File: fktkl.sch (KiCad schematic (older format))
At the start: 157 parts, among them K1 Esc, K10 Super, K11 2, K12 W, K13 S, K14 X, K15 Alt, K16 3, K17 E, K18 D, K19 C, K2 Tab, K20 4, K21 R, K22 F, K23 V, K24 5, K25 T, K26 G, K27 B, K28 6, K29 Y, K3 Caps, K3.1 SCaps, K30 H, K31 N, K32 Space, K33 7, K34 U, K35 J, K36 M, K37 8, K38 I, K39 K, K4 Shift, K40 ,, K41 9, K42 O, K43 L, K44 ., K45 0, K46 P, K47 ;, K48 /, K49 Ctrl, K5 Ctrl, K50 -, K51 [, K52 ', K53 =, K54 ], K55 Shift, K56 Win, K57 Yen, K58 BS1, K59 BS2, K6 1, K60 \\, K61 Enter, K62 Fn, K63 AltGr, K64 Ins, K65 Del, K66 C0, K67 C3, K68 Left, K69 Home, K7 Q, K70 End, K71 C1, K72 Up, K73 Down, K74 PgUp, K75 PgDwn, K76 C2, K77 C4, K78 Right, K8 A, K9 Z, U1 TEENSY2.0

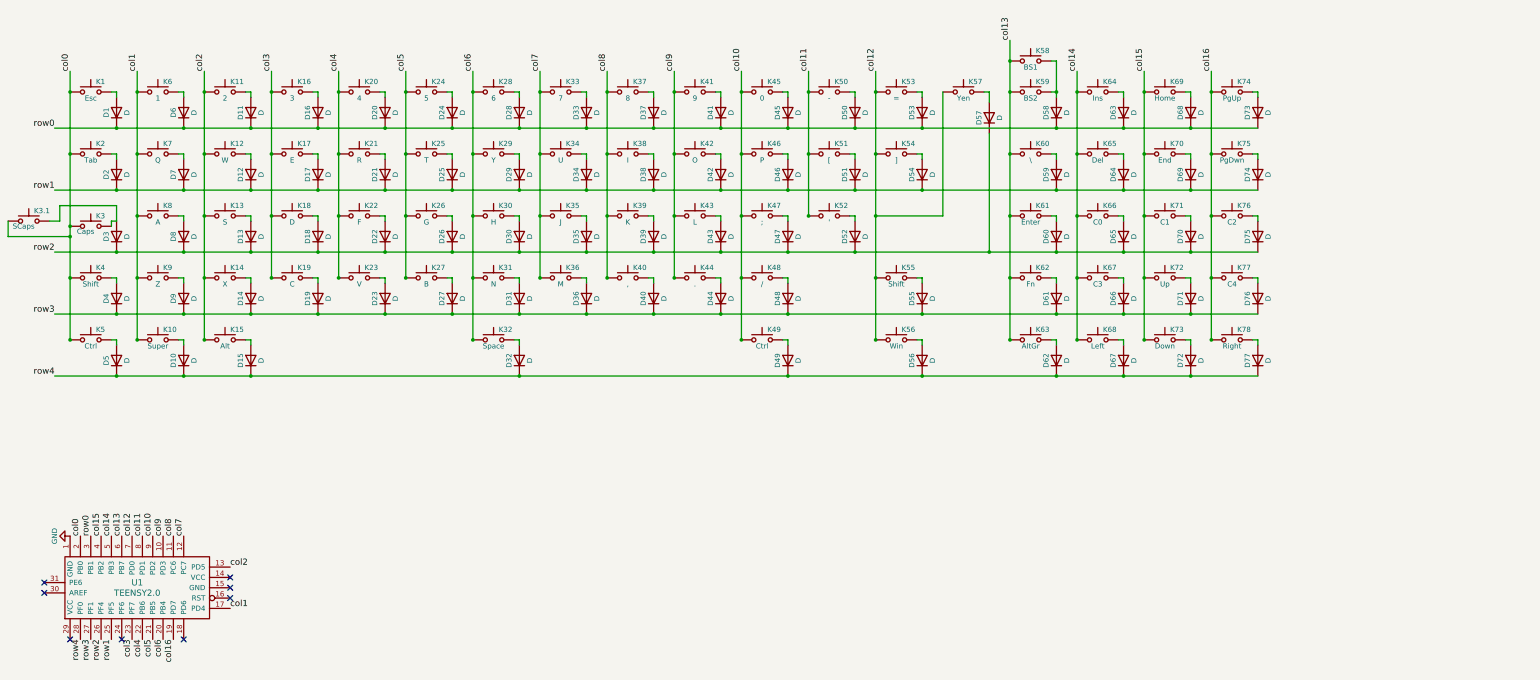
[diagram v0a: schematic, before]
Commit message: changed controller to pro micro
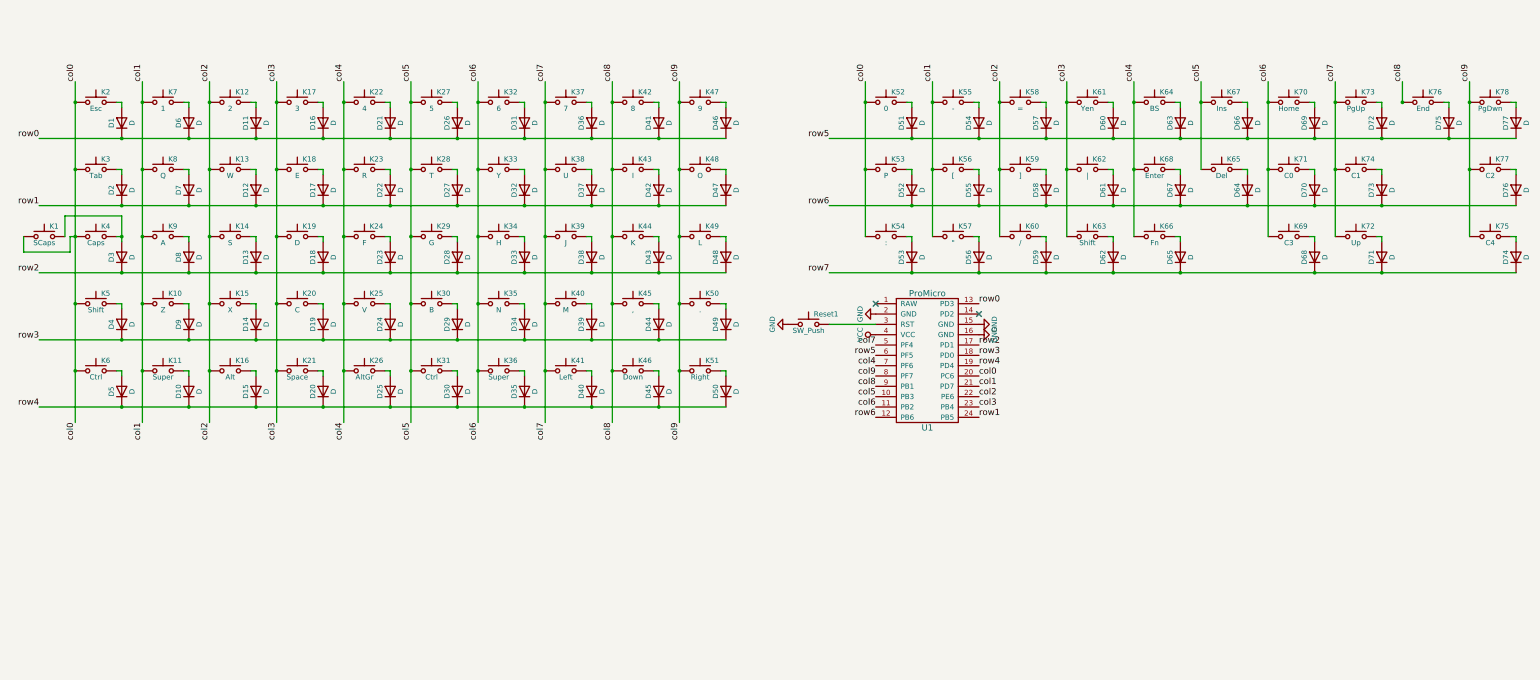
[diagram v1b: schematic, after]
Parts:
- removed K3.1: SCaps, canadian_footprints:Mx_Alps_125, symbol SW_Push
- removed U1: TEENSY2.0, jan_footprints:Teensy_20_wo_front_text, symbol TEENSY2.0
- added Reset1: SW_Push, canadian_footprints:SW_TACT_ALPS_SKQGABE010, symbol SW_Push
- added U1: ProMicro, canadian_footprints:Pro_Micro, symbol ProMicro
- K1: value Esc -> SCaps; footprint canadian_footprints:Mx_Alps_100 -> canadian_footprints:Mx_Alps_125
- K10: value Super -> Z
- K11: value 2 -> Super
- K12: value W -> 2
- K13: value S -> W
- K14: value X -> S
- K15: value Alt -> X; footprint canadian_footprints:Mx_Alps_150 -> canadian_footprints:Mx_Alps_100
- K16: value 3 -> Alt; footprint canadian_footprints:Mx_Alps_100 -> canadian_footprints:Mx_Alps_150
- K17: value E -> 3
- K18: value D -> E
- K19: value C -> D
- K2: value Tab -> Esc; footprint canadian_footprints:Mx_Alps_150 -> canadian_footprints:Mx_Alps_100
- K20: value 4 -> C
- K21: value R -> Space; footprint canadian_footprints:Mx_Alps_100 -> MX_Alps_Hybrid:MX-7U-ReversedStabilizers-NoLED
- K22: value F -> 4
- K23: value V -> R
- K24: value 5 -> F
- K25: value T -> V
- K26: value G -> AltGr; footprint canadian_footprints:Mx_Alps_100 -> canadian_footprints:Mx_Alps_150
- K27: value B -> 5
- K28: value 6 -> T
- K29: value Y -> G
- K3: value Caps -> Tab; footprint canadian_footprints:Mx_Alps_175 -> canadian_footprints:Mx_Alps_150
- K30: value H -> B
- K31: value N -> Ctrl; footprint canadian_footprints:Mx_Alps_100 -> canadian_footprints:Mx_Alps_150
- K32: value Space -> 6; footprint MX_Alps_Hybrid:MX-7U-ReversedStabilizers-NoLED -> canadian_footprints:Mx_Alps_100
- K33: value 7 -> Y
- K34: value U -> H
- K35: value J -> N
- K36: value M -> Super
- K37: value 8 -> 7
- K38: value I -> U
- K39: value K -> J
- K4: value Shift -> Caps; footprint canadian_footprints:Mx_Alps_225 -> canadian_footprints:Mx_Alps_175
- K40: value , -> M
- K41: value 9 -> Left
- K42: value O -> 8
- K43: value L -> I
- K44: value . -> K
- K45: value 0 -> ,
- K46: value P -> Down
- K47: value ; -> 9
- K48: value / -> O
- K49: value Ctrl -> L; footprint canadian_footprints:Mx_Alps_150 -> canadian_footprints:Mx_Alps_100
- K5: value Ctrl -> Shift; footprint canadian_footprints:Mx_Alps_150 -> canadian_footprints:Mx_Alps_225
- K50: value - -> .
- K51: value [ -> Right
- K52: value ' -> 0
- K53: value = -> P
- K54: value ] -> :
- K55: value Shift -> -; footprint canadian_footprints:Mx_Alps_175 -> canadian_footprints:Mx_Alps_100
- K56: value Win -> [
- K57: value Yen -> \"
- K58: value BS1 -> =
- K59: value BS2 -> ]; footprint canadian_footprints:Mx_Alps_200 -> canadian_footprints:Mx_Alps_100
- K6: value 1 -> Ctrl; footprint canadian_footprints:Mx_Alps_100 -> canadian_footprints:Mx_Alps_150
- K60: value \\ -> /; footprint canadian_footprints:Mx_Alps_150 -> canadian_footprints:Mx_Alps_100
- K61: value Enter -> Yen; footprint canadian_footprints:Mx_Alps_225 -> canadian_footprints:Mx_Alps_100
- K62: value Fn -> |; footprint canadian_footprints:Mx_Alps_100 -> canadian_footprints:Mx_Alps_150
- K63: value AltGr -> Shift; footprint canadian_footprints:Mx_Alps_150 -> canadian_footprints:Mx_Alps_175
- K64: value Ins -> BS
- K66: value C0 -> Fn
- K67: value C3 -> Ins
- K68: value Left -> Enter; footprint canadian_footprints:Mx_Alps_100 -> canadian_footprints:Mx_Alps_225
- K69: value Home -> C3
- K7: value Q -> 1
- K70: value End -> Home
- K71: value C1 -> C0
- K73: value Down -> PgUp
- K74: value PgUp -> C1
- K75: value PgDwn -> C4
- K76: value C2 -> End
- K77: value C4 -> C2
- K78: value Right -> PgDwn
- K8: value A -> Q
- K9: value Z -> A
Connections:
- net GND: now also Reset1.1, U1.15 (GND), U1.16 (GND), U1.2 (GND)
- net col0: now also K52.1, K53.1, K54.1, K6.1, U1.20 (PC6)
- net col1: now also K11.1, K55.1, K56.1, K57.1, U1.21 (PD7); no longer K6.1
- net col2: now also K16.1, K58.1, K59.1, K60.1, U1.22 (PE6); no longer K11.1
- net col3: now also K20.1, K21.1, K61.1, K62.1, K63.1, U1.23 (PB4); no longer K16.1
- net col4: now also K24.1, K25.1, K26.1, K64.1, K66.1, K68.1, U1.7 (PF6); no longer K20.1, K21.1
- net col5: now also K28.1, K29.1, K30.1, K31.1, K65.1, K67.1, U1.10 (PB3); no longer K24.1, K25.1, K26.1
- net col6: now also K33.1, K34.1, K35.1, K36.1, K69.1, K70.1, K71.1, U1.11 (PB2); no longer K28.1, K29.1, K30.1, K31.1
- net col7: now also K37.1, K38.1, K39.1, K40.1, K41.1, K72.1, K73.1, K74.1, U1.5 (PF4); no longer K33.1, K34.1, K35.1, K36.1
- net col8: now also K42.1, K43.1, K44.1, K45.1, K46.1, K76.1, U1.9 (PB1); no longer K37.1, K38.1, K39.1, K40.1
- net col9: now also K47.1, K48.1, K49.1, K50.1, K51.1, K75.1, K77.1, K78.1, U1.8 (PF7); no longer K41.1, K42.1, K43.1, K44.1
- net row0: now also D21.1 (K), D26.1 (K), D31.1 (K), D36.1 (K), D46.1 (K), U1.13 (PD3); no longer D20.1 (K), D24.1 (K), D28.1 (K), D33.1 (K), D37.1 (K), D45.1 (K), D50.1 (K), D53.1 (K), D58.1 (K), D63.1 (K), D68.1 (K), D73.1 (K)
- net row1: now also D22.1 (K), D27.1 (K), D32.1 (K), D37.1 (K), D47.1 (K), U1.24 (PB5); no longer D21.1 (K), D25.1 (K), D29.1 (K), D34.1 (K), D38.1 (K), D46.1 (K), D51.1 (K), D54.1 (K), D59.1 (K), D64.1 (K), D69.1 (K), D74.1 (K)
- net row2: now also D23.1 (K), D28.1 (K), D33.1 (K), D38.1 (K), D48.1 (K), U1.17 (PD1); no longer D22.1 (K), D26.1 (K), D30.1 (K), D35.1 (K), D39.1 (K), D47.1 (K), D52.1 (K), D57.1 (K), D60.1 (K), D65.1 (K), D70.1 (K), D75.1 (K)
- net row3: now also D24.1 (K), D29.1 (K), D34.1 (K), D39.1 (K), D49.1 (K), U1.18 (PD0); no longer D23.1 (K), D27.1 (K), D31.1 (K), D36.1 (K), D40.1 (K), D48.1 (K), D55.1 (K), D61.1 (K), D66.1 (K), D71.1 (K), D76.1 (K)
- net row4: now also D20.1 (K), D25.1 (K), D30.1 (K), D35.1 (K), D40.1 (K), D45.1 (K), D50.1 (K), U1.19 (PD4); no longer D32.1 (K), D49.1 (K), D56.1 (K), D62.1 (K), D67.1 (K), D72.1 (K), D77.1 (K)
- net at K2.2: now also D1.2 (A); no longer D2.2 (A)
- net at K1.2: now also D3.2 (A), K4.2; no longer D1.2 (A)
- net at D4.2 (A): now also K5.2; no longer K4.2
- net at K3.2: now also D2.2 (A); no longer D3.2 (A)
- net at D5.2 (A): now also K6.2; no longer K5.2
- net at K7.2: now also D6.2 (A); no longer D7.2 (A)
- net at K9.2: now also D8.2 (A); no longer D9.2 (A)
- net at K8.2: now also D7.2 (A); no longer D8.2 (A)
- net at K10.2: now also D9.2 (A); no longer D10.2 (A)
- net at K12.2: now also D11.2 (A); no longer D12.2 (A)
- net at K11.2: now also D10.2 (A); no longer D11.2 (A)
- net at K14.2: now also D13.2 (A); no longer D14.2 (A)
- net at K13.2: now also D12.2 (A); no longer D13.2 (A)
- net at K15.2: now also D14.2 (A); no longer D15.2 (A)
- net at K17.2: now also D16.2 (A); no longer D17.2 (A)
- net at K16.2: now also D15.2 (A); no longer D16.2 (A)
- net at K19.2: now also D18.2 (A); no longer D19.2 (A)
- net at K18.2: now also D17.2 (A); no longer D18.2 (A)
- net at D21.2 (A): now also K22.2; no longer K21.2
- net at K20.2: now also D19.2 (A); no longer D20.2 (A)
- net at K23.2: now also D22.2 (A); no longer D23.2 (A)
- net at K25.2: now also D24.2 (A); no longer D25.2 (A)
- net at K24.2: now also D23.2 (A); no longer D24.2 (A)
- net at K27.2: now also D26.2 (A); no longer D27.2 (A)
- net at K26.2: now also D25.2 (A); no longer D26.2 (A)
- net at K29.2: now also D28.2 (A); no longer D29.2 (A)
- net at K28.2: now also D27.2 (A); no longer D28.2 (A)
- net at D31.2 (A): now also K32.2; no longer K31.2
- net at K30.2: now also D29.2 (A); no longer D30.2 (A)
- net at D32.2 (A): now also K33.2; no longer K32.2
- net at K34.2: now also D33.2 (A); no longer D34.2 (A)
- net at D36.2 (A): now also K37.2; no longer K36.2
- net at K35.2: now also D34.2 (A); no longer D35.2 (A)
- net at K38.2: now also D37.2 (A); no longer D38.2 (A)
- net at K40.2: now also D39.2 (A); no longer D40.2 (A)
- net at K39.2: now also D38.2 (A); no longer D39.2 (A)
- net at K42.2: now also D41.2 (A); no longer D42.2 (A)
- net at K41.2: now also D40.2 (A); no longer D41.2 (A)
- net at K44.2: now also D43.2 (A); no longer D44.2 (A)
- net at K43.2: now also D42.2 (A); no longer D43.2 (A)
- net at D46.2 (A): now also K47.2; no longer K46.2
- net at K45.2: now also D44.2 (A); no longer D45.2 (A)
- net at K48.2: now also D47.2 (A); no longer D48.2 (A)
- net at K49.2: now also D48.2 (A); no longer D49.2 (A)
- net at D51.2 (A): now also K52.2; no longer K51.2
- net at K50.2: now also D49.2 (A); no longer D50.2 (A)
- net at D52.2 (A): now also K53.2; no longer K52.2
- net at K54.2: now also D53.2 (A); no longer D54.2 (A)
- net at D55.2 (A): now also K56.2; no longer K55.2
- net at D56.2 (A): now also K57.2; no longer K56.2
- net at D57.2 (A): now also K58.2; no longer K57.2
- net at D58.2 (A), K59.2: no longer K58.2
- removed net col10: K45.1, K46.1, K47.1, K48.1, K49.1
- removed net col11: K50.1, K51.1, K52.1
- removed net col12: K53.1, K54.1, K55.1, K56.1, K57.1
- removed net col13: K58.1, K59.1, K60.1, K61.1, K62.1, K63.1
- removed net col14: K64.1, K65.1, K66.1, K67.1, K68.1
- removed net col15: K69.1, K70.1, K71.1, K72.1, K73.1
- removed net col16: K74.1, K75.1, K76.1, K77.1, K78.1
- new net: Reset1.2, U1.3 (RST)
- new net: D20.2 (A), K21.2
- new net: D54.2 (A), K55.2
- new net: D30.2 (A), K31.2
- new net: D35.2 (A), K36.2
- new net: D45.2 (A), K46.2
- new net: D50.2 (A), K51.2
- new net VCC: U1.4 (VCC)
- new net row5: D51.1 (K), D54.1 (K), D57.1 (K), D60.1 (K), D63.1 (K), D66.1 (K), D69.1 (K), D72.1 (K), D75.1 (K), D77.1 (K), U1.6 (PF5)
- new net row6: D52.1 (K), D55.1 (K), D58.1 (K), D61.1 (K), D64.1 (K), D67.1 (K), D70.1 (K), D73.1 (K), D76.1 (K), U1.12 (PB6)
- new net row7: D53.1 (K), D56.1 (K), D59.1 (K), D62.1 (K), D65.1 (K), D68.1 (K), D71.1 (K), D74.1 (K)
- no-connect marks 8 -> 2

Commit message: connected row7
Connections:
- net row7: now also U1.14 (PD2)
- no-connect marks 2 -> 1
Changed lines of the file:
@@
 Text Label 9200 4100 2    60   ~ 0
 col4
-NoConn ~ 10200 3600
 NoConn ~ 9200 3500
 $Comp
@@
 Text Label 9100 1350 1    60   ~ 0
 col0
+Text Label 10200 3600 0    60   ~ 0
+row7
 $EndSCHEMATC

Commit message: switche left ctrl and left gui
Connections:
- net col5: now also K36.1; no longer K31.1
- net col6: now also K31.1; no longer K36.1
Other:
- moved on the sheet: D30, D35, K31, K36
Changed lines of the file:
@@
 L D D30
 U 1 1 5B1ACA93
+P 5800 4350
+F 0 "D30" H 5800 4450 50  0000 C CNN
+F 1 "D" H 5800 4250 50  0000 C CNN
+F 2 "keyboard_parts:D_SOD123_axial" H 5800 4350 50  0001 C CNN
+F 3 "" H 5800 4350 50  0001 C CNN
+	1    5800 4350
+	0    -1   -1   0
+$EndComp
+$Comp
+L SW_Push K31
+U 1 1 5B1ACA99
+P 5550 4150
+F 0 "K31" H 5600 4250 50  0000 L CNN
+F 1 "Ctrl" H 5550 4090 50  0000 C CNN
+F 2 "canadian_footprints:Mx_Alps_150" H 5550 4350 50  0001 C CNN
+F 3 "" H 5550 4350 50  0001 C CNN
+	1    5550 4150
+	1    0    0    -1
+$EndComp
+Wire Wire Line
+	5750 4150 5800 4150
+Wire Wire Line
+	5800 4150 5800 4200
+Connection ~ 4700 4150
+$Comp
+L D D35
+U 1 1 5B1AD372
 P 5150 4350
-F 0 "D30" H 5150 4450 50  0000 C CNN
+F 0 "D35" H 5150 4450 50  0000 C CNN
 F 1 "D" H 5150 4250 50  0000 C CNN
 F 2 "keyboard_parts:D_SOD123_axial" H 5150 4350 50  0001 C CNN
@@
 $EndComp
 $Comp
-L SW_Push K31
-U 1 1 5B1ACA99
+L SW_Push K36
+U 1 1 5B1AD378
 P 4900 4150
-F 0 "K31" H 4950 4250 50  0000 L CNN
-F 1 "Ctrl" H 4900 4090 50  0000 C CNN
-F 2 "canadian_footprints:Mx_Alps_150" H 4900 4350 50  0001 C CNN
+F 0 "K36" H 4950 4250 50  0000 L CNN
+F 1 "Super" H 4900 4090 50  0000 C CNN
+F 2 "canadian_footprints:Mx_Alps_100" H 4900 4350 50  0001 C CNN
 F 3 "" H 4900 4350 50  0001 C CNN
 	1    4900 4150
@@
 Wire Wire Line
 	5150 4150 5150 4200
-Connection ~ 4700 4150
-$Comp
-L D D35
-U 1 1 5B1AD372
-P 5800 4350
-F 0 "D35" H 5800 4450 50  0000 C CNN
-F 1 "D" H 5800 4250 50  0000 C CNN
-F 2 "keyboard_parts:D_SOD123_axial" H 5800 4350 50  0001 C CNN
-F 3 "" H 5800 4350 50  0001 C CNN
-	1    5800 4350
-	0    -1   -1   0
-$EndComp
-$Comp
-L SW_Push K36
-U 1 1 5B1AD378
-P 5550 4150
-F 0 "K36" H 5600 4250 50  0000 L CNN
-F 1 "Super" H 5550 4090 50  0000 C CNN
-F 2 "canadian_footprints:Mx_Alps_100" H 5550 4350 50  0001 C CNN
-F 3 "" H 5550 4350 50  0001 C CNN
-	1    5550 4150
-	1    0    0    -1
-$EndComp
-Wire Wire Line
-	5750 4150 5800 4150
-Wire Wire Line
-	5800 4150 5800 4200
 Connection ~ 5350 4150
 $Comp
